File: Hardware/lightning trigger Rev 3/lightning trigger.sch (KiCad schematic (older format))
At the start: 70 parts, among them J1 Conn_02x03_Odd_Even, J2 Conn_01x04, J3 SJ-2523-SMT, J4 SJ-2523-SMT, J5 SJ-2523-SMT, J6 SJ-2523-SMT, J7 USB_OTG, J8 Conn_01x02_Female, J9 Conn_01x02, Q1 Q_Photo_NPN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

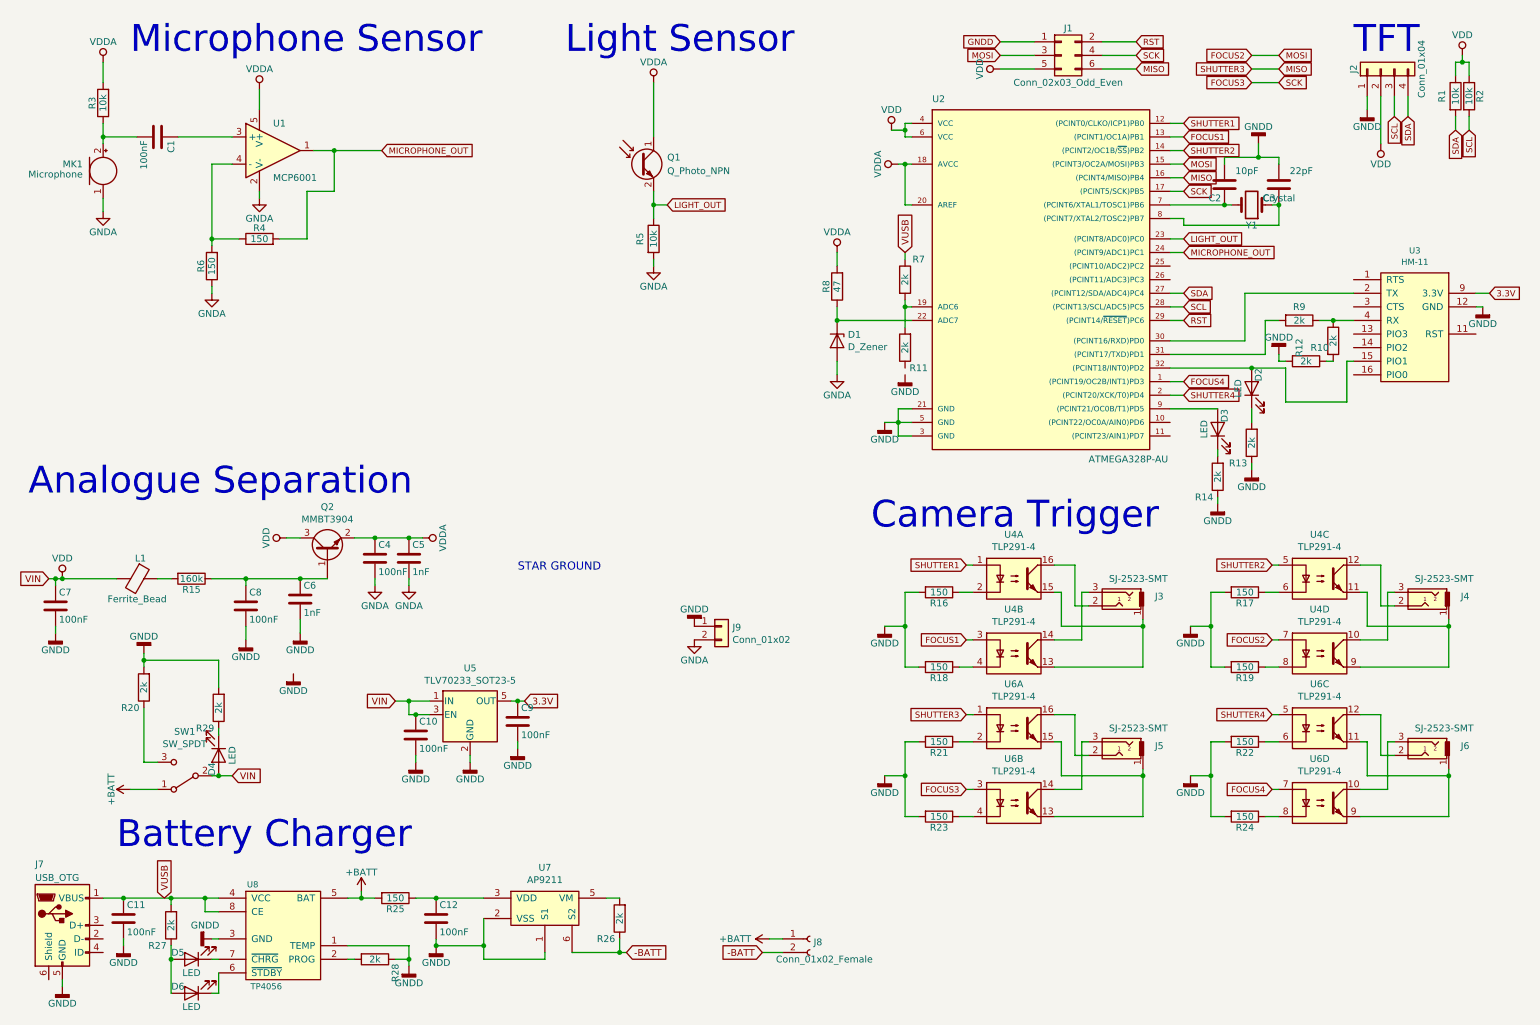
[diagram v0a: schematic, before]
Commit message: optimising DFM. removed 150 ohm resistors and replaced with 2k that are already in use. Added hardware to reset uC from HM-11. Fixed BATT- and GND issue with AP9211 that was causing the battery to still be connected below 3V. Connected TX pin on uC (pin 30) to external interrupt pin (INT0 PIN 32).
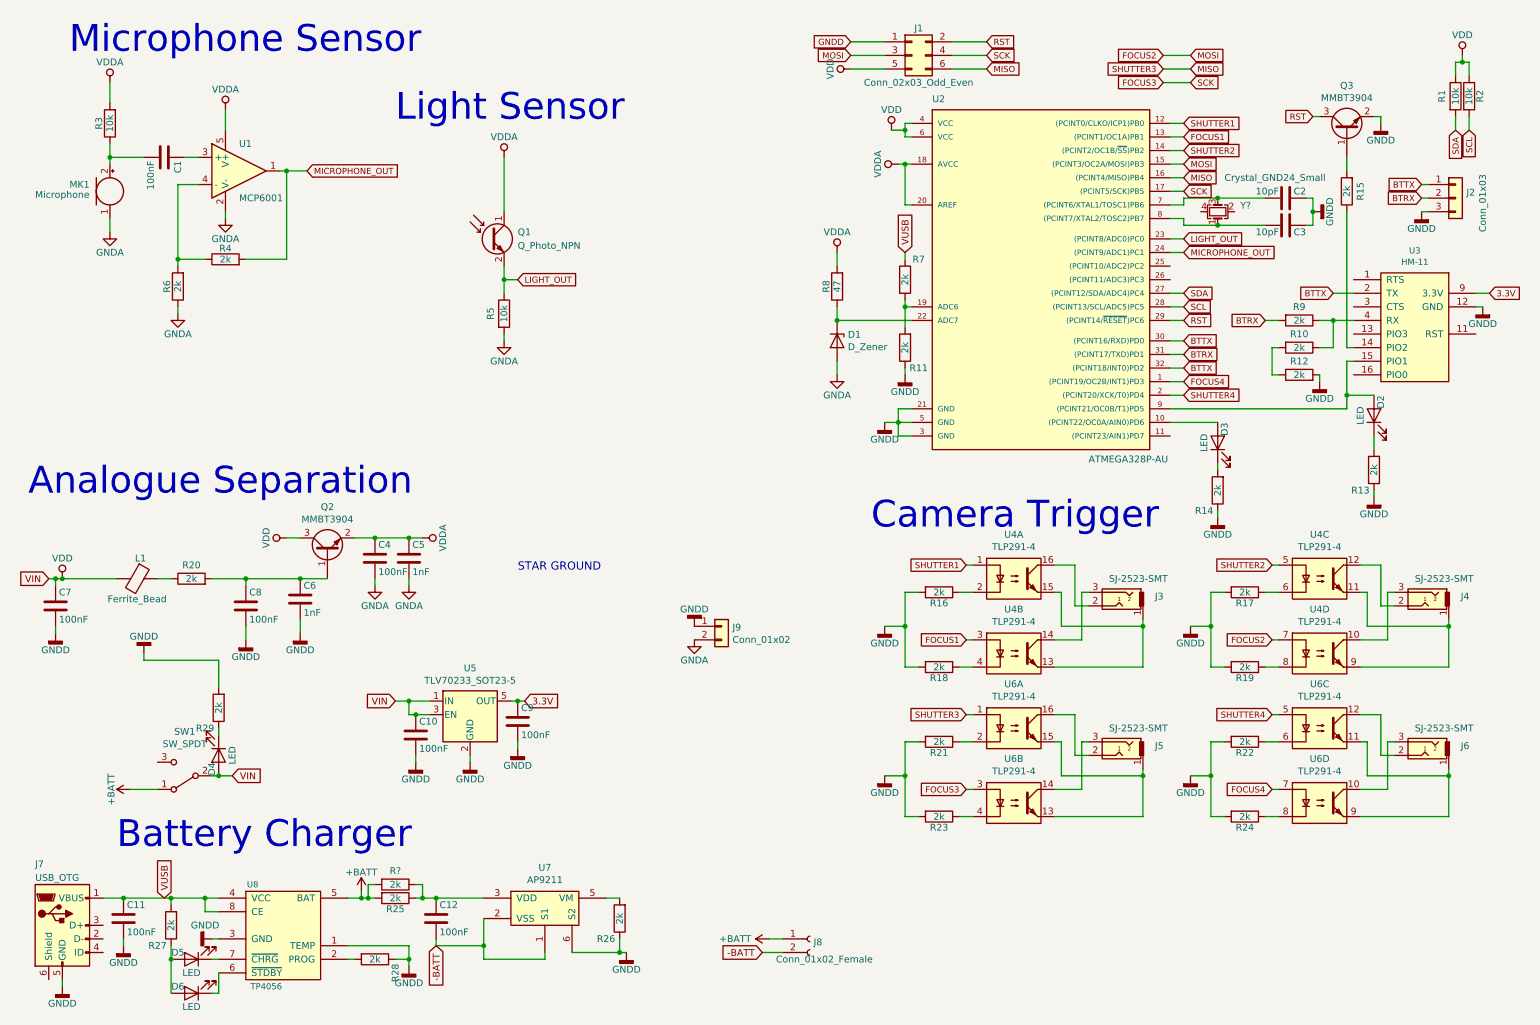
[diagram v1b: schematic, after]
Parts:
- removed J2: Conn_01x04, Pin_Headers:Pin_Header_Straight_1x04_Pitch2.54mm, symbol conn:Conn_01x04
- removed Y1: Crystal, Crystal:Crystal_SMD_2016-4Pin_2.0x1.6mm, symbol Device:Crystal
- added J2: Conn_01x03, symbol audio_conn:Conn_01x03
- added Q3: MMBT3904, Package_TO_SOT_SMD:SOT-23, symbol Transistor_BJT:MMBT3904
- added R?: 2k, Resistor_SMD:R_0603_1608Metric, symbol Device:R
- added Y?: Crystal_GND24_Small, Crystal:Crystal_SMD_2016-4Pin_2.0x1.6mm, symbol Device:Crystal_GND24_Small
- C3: value 22pF -> 10pF
- R15: value 160k -> 2k; Manufacturer Part Number ERJ-3GEYJ164V -> ERJ-3GEYJ202V
- R16, R17, R18, R19, R21, R22, R23, R24, R25, R4, R6: value 150 -> 2k; Manufacturer Part Number ERJ-3GEYJ151V -> ERJ-3GEYJ202V
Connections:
- net +BATT: now also R?.2
- net -BATT: now also C12.2, U7.1 (S1), U7.2 (VSS); no longer R26.1, U7.6 (S2)
- net GNDD: now also R11.1, R26.1, U7.6 (S2), J2.3 (Pin_3), Q3.2 (E); no longer C12.2, R20.2, U7.1 (S1), U7.2 (VSS)
- net RST: now also Q3.3 (C)
- net at U2.10 ((PCINT22/OC0A/AIN0)PD6): now also D3.2 (A)
- net BTTX: now reaches U2.30 ((PCINT16/RXD)PD0), U3.2 (TX)
- net BTTX: now also U2.32 ((PCINT18/INT0)PD2), J2.1 (Pin_1)
- net BTRX: now reaches R9.2, U2.31 ((PCINT17/TXD)PD1)
- net BTRX: now also J2.2 (Pin_2)
- net at D2.2 (A), U3.15 (PIO1): now also U2.9 ((PCINT21/OC0B/T1)PD5); no longer U2.32 ((PCINT18/INT0)PD2)
- net at C2.1, U2.7 ((PCINT6/XTAL1/TOSC1)PB6): now also Y?.3
- net at C3.1, U2.8 ((PCINT7/XTAL2/TOSC2)PB7): now also Y?.1
- net at C6.1, C8.1, Q2.1 (B): now also R20.2; no longer R15.1
- net at L1.1: now also R20.1; no longer R15.2
- net at C12.1, R25.1, U7.3 (VDD): now also R?.1
- net at SW1.3 (C): no longer R20.1
- net at U3.14 (PIO2): now also R15.1
- new net: Q3.1 (B), R15.2
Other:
- note removed: "TFT"
- moved on the sheet: C1, C2, C3, D2, D3, J1, MK1, Q1, R10, R12, R13, R14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
